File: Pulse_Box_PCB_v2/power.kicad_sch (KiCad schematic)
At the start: 30 parts, among them J1 Screw_Terminal_01x02, U3 TPS54560BDDA, U4 AP2112K-3.3, U5 74LVC1G3157

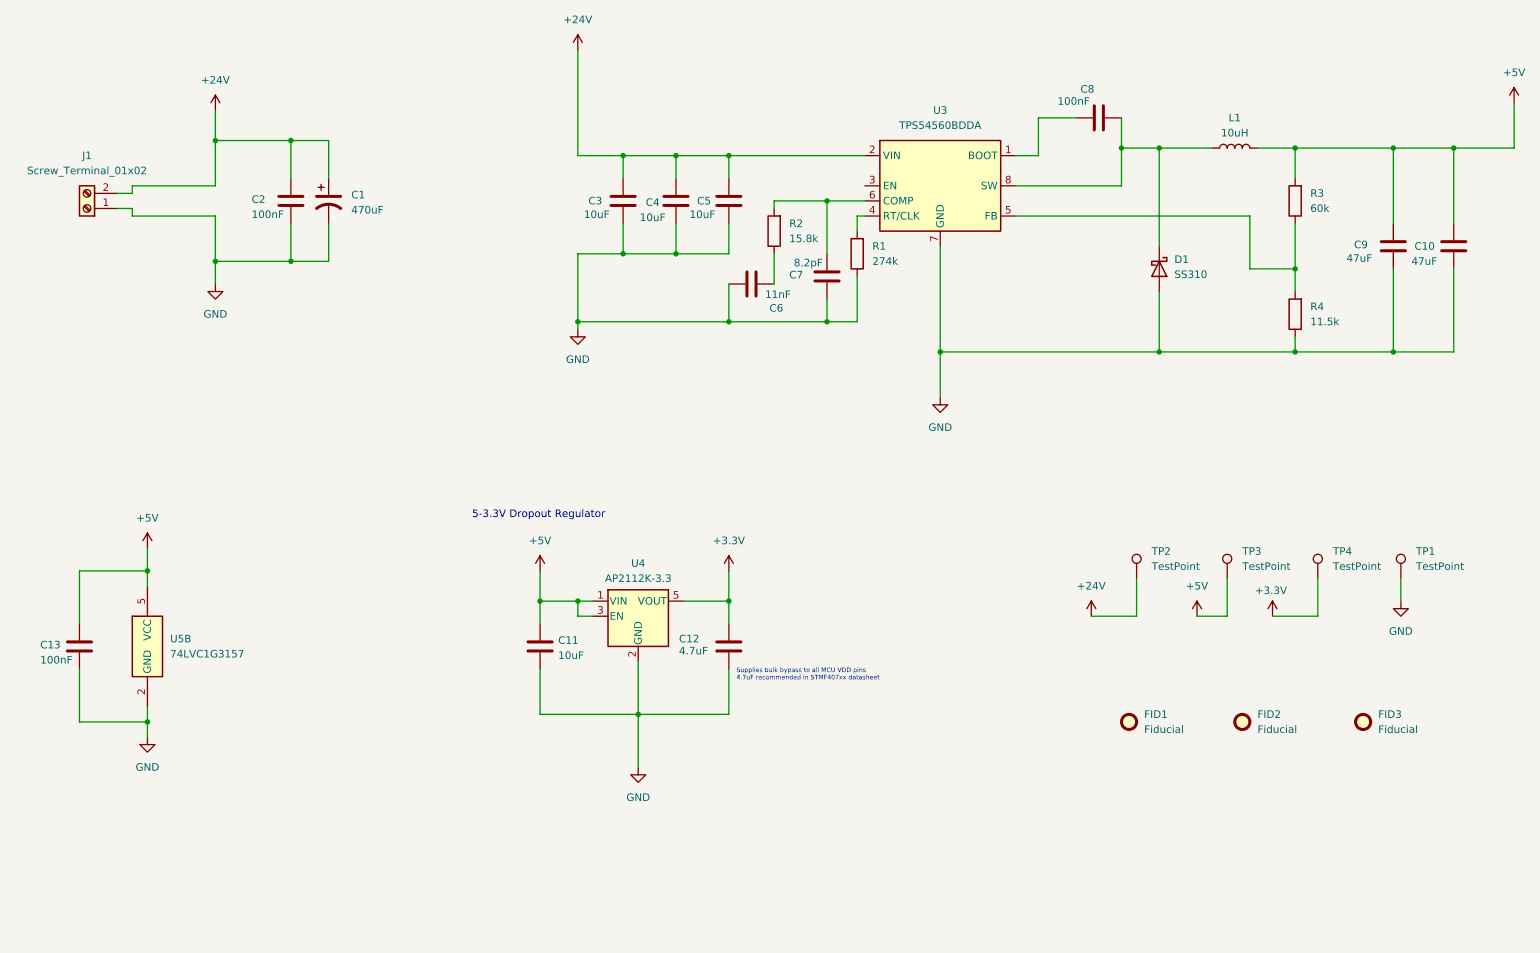
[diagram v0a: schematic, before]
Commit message: add design for pulsebox panel, update v2 PCB to remove 485 trans
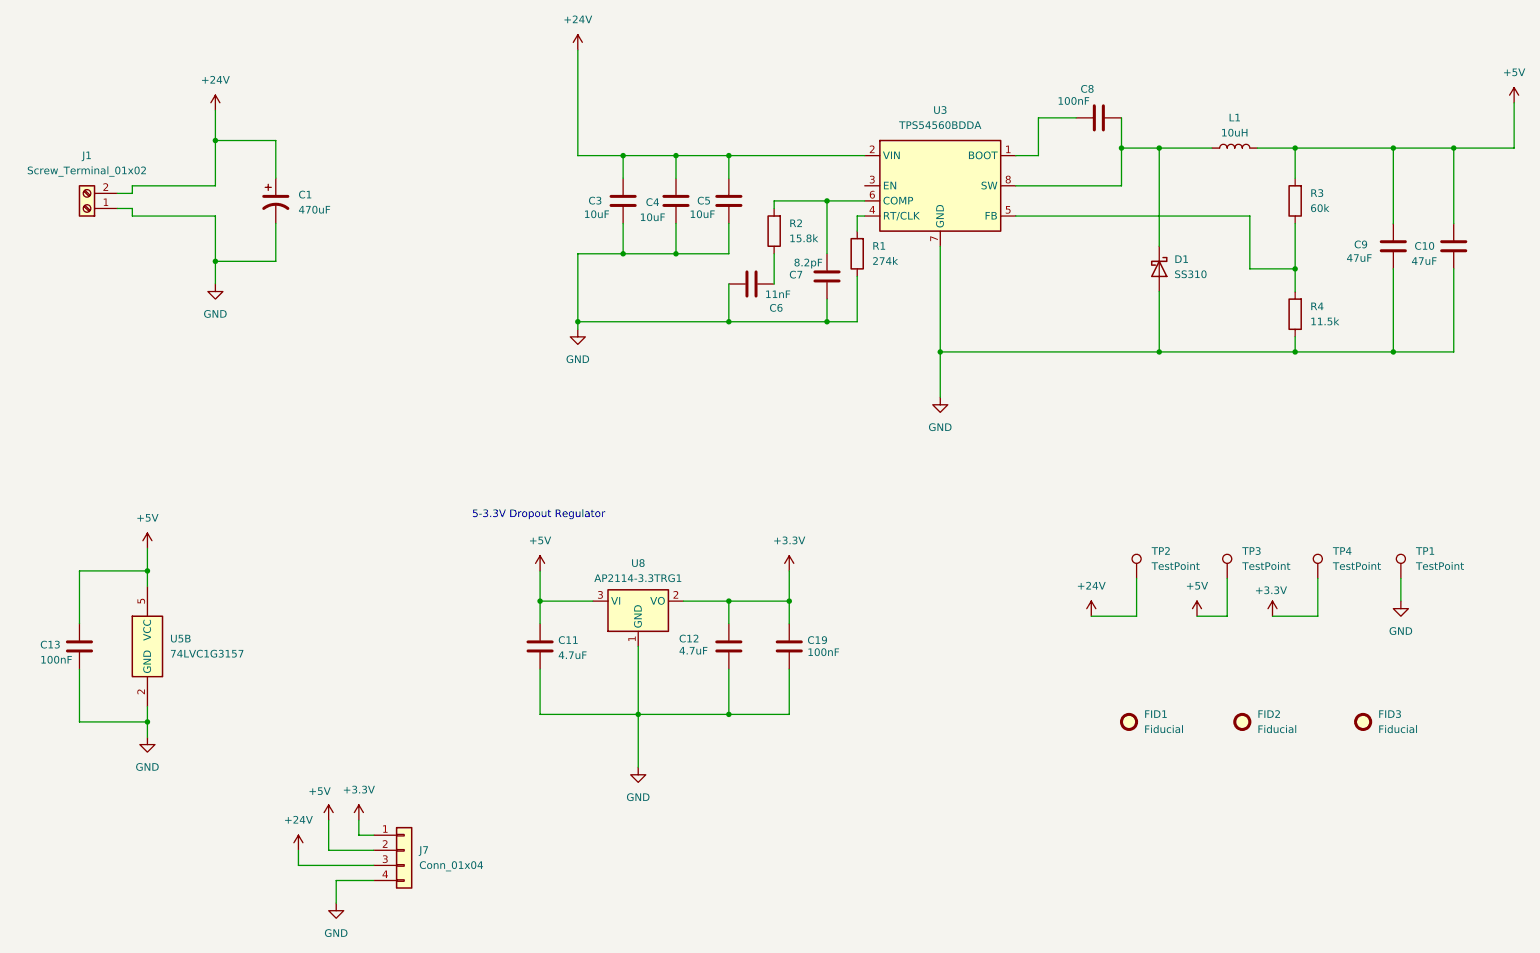
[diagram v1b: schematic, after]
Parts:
- removed C2: 100nF, Capacitor_SMD:C_0402_1005Metric, symbol Device:C
- removed U4: AP2112K-3.3, Package_TO_SOT_SMD:SOT-23-5, symbol Regulator_Linear:AP2112K-3.3
- added C19: 100nF, Capacitor_SMD:C_0402_1005Metric, symbol Device:C
- added J7: Conn_01x04, Connector_PinHeader_2.54mm:PinHeader_1x04_P2.54mm_Vertical, symbol Connector_Generic:Conn_01x04
- added U8: AP2114-3.3TRG1, Package_TO_SOT_SMD:SOT-223-3_TabPin2, symbol Regulator_Linear:AP1117-33
- C11: value 10uF -> 4.7uF; JLCPCB Part # C440198 -> C1779
- C6: footprint Capacitor_SMD:C_1206_3216Metric -> Capacitor_SMD:C_0805_2012Metric; JLCPCB Part # C2171071 -> C710944
- U5: footprint (none) -> Package_TO_SOT_SMD:SOT-23-6; JLCPCB Part # C52140494 -> C10426
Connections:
- net +24V: now also J7.3 (Pin_3)
- net +3.3V: now also C19.1, J7.1 (Pin_1), U8.2 (VO)
- net +5V: now also J7.2 (Pin_2), U8.3 (VI)
- net GND: now also C19.2, J7.4 (Pin_4), U8.1 (GND)
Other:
- note removed: "Supplies bulk bypass to all MCU VDD pins 4.7uF recommended in STMF407xx datasheet"
- moved on the sheet: C1

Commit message: complete v2 and v1 panel design, this is the final design sent to jlcpcb for v2
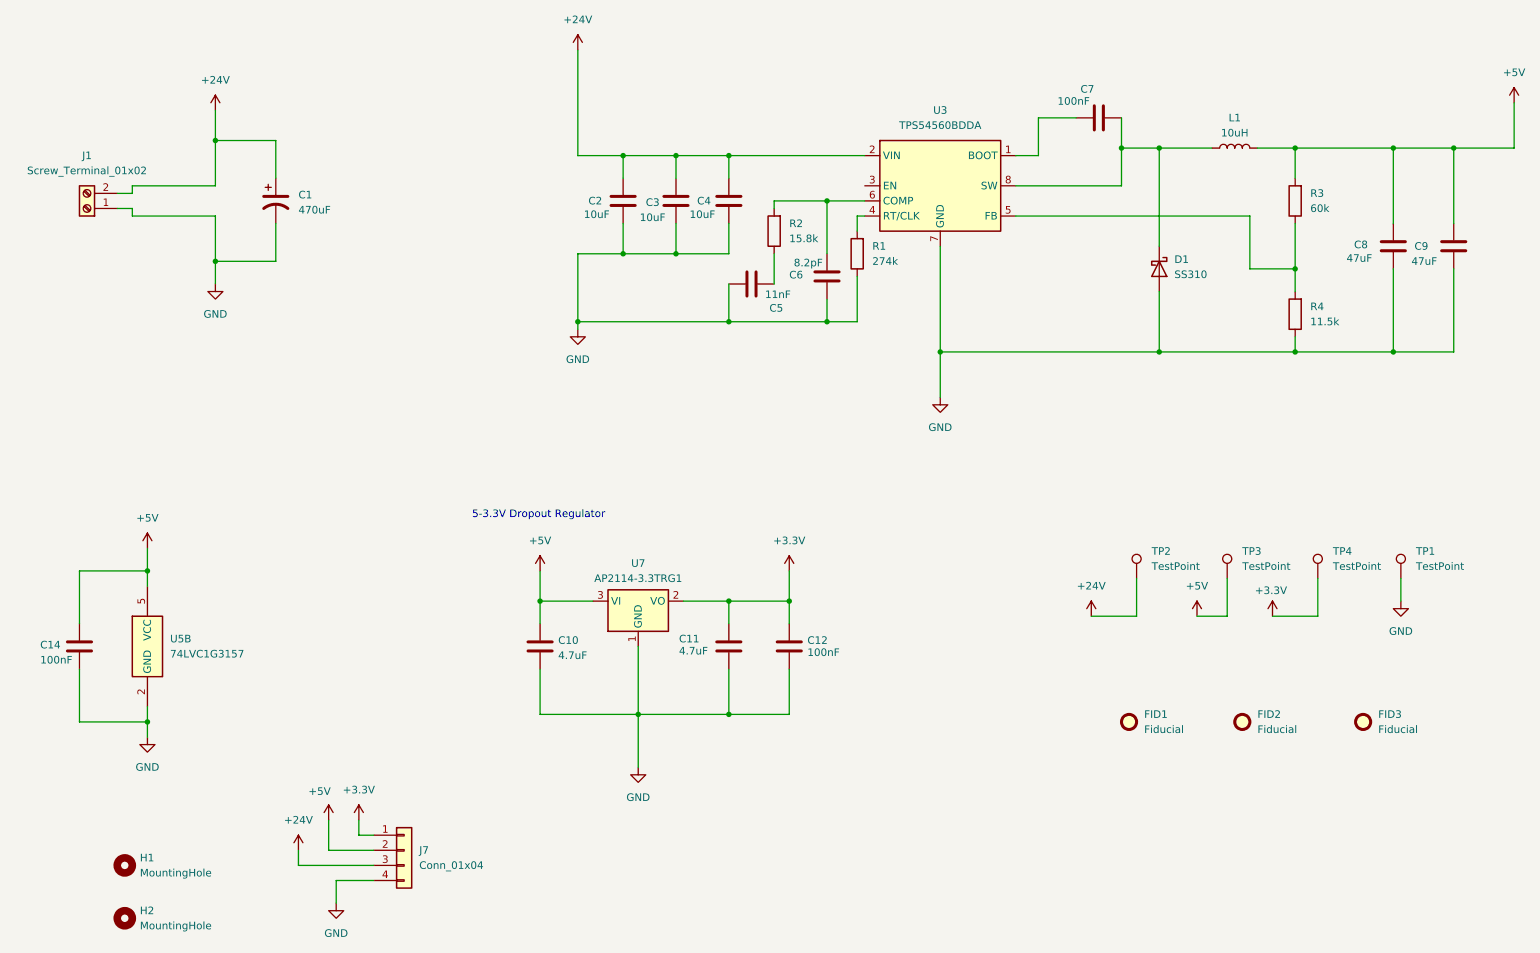
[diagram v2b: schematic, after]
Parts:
- added H1, H2: MountingHole, MountingHole:MountingHole_3.2mm_M3, symbol Mechanical:MountingHole
- L1: footprint Inductor_SMD:L_APV_APH1030 -> Inductor_SMD:L_TechFuse_SL1040
- renumbered C11 to C10, C12 to C11, C19 to C12, C13 to C14, C3 to C2, C4 to C3, C5 to C4, C6 to C5, C7 to C6, C8 to C7, C9 to C8, C10 to C9, U8 to U7
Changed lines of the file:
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@@
 	)
 	(symbol
+		(lib_id "Mechanical:MountingHole")
+		(at 39.37 173.99 0)
+		(unit 1)
+		(exclude_from_sim no)
+		(in_bom no)
+		(on_board yes)
+		(dnp no)
+		(fields_autoplaced yes)
+		(property "Reference" "H1"
+			(at 41.91 172.7199 0)
+			(effects
+				(font
+					(size 1.27 1.27)
+				)
+				(justify left)
+			)
+		)
+		(property "Value" "MountingHole"
+			(at 41.91 175.2599 0)
+			(effects
+				(font
+					(size 1.27 1.27)
+				)
+				(justify left)
+			)
+		)
+		(property "Footprint" "MountingHole:MountingHole_3.2mm_M3"
+			(at 39.37 173.99 0)
+			(effects
+				(font
+					(size 1.27 1.27)
+				)
+				(hide yes)
+			)
+		)
+		(property "Datasheet" "~"
+			(at 39.37 173.99 0)
+			(effects
+				(font
+					(size 1.27 1.27)
+				)
+				(hide yes)
+			)
+		)
+		(property "Description" "Mounting Hole without connection"
+			(at 39.37 173.99 0)
+			(effects
+				(font
+					(size 1.27 1.27)
+				)
+				(hide yes)
+			)
+		)
+		(instances
+			(project ""
+				(path "/ef0e555f-a8f1-4b4b-84db-9e9da0748d24/ac0dde2f-bbaa-42bf-826d-318675a6462a"
+					(reference "H1")
+					(unit 1)
+				)
+			)
+		)
+	)
+	(symbol
 		(lib_id "power:+5V")
 		(at 73.66 166.37 0)
@@
 	)
 	(symbol
+		(lib_id "Mechanical:MountingHole")
+		(at 39.37 182.88 0)
+		(unit 1)
+		(exclude_from_sim no)
+		(in_bom no)
+		(on_board yes)
+		(dnp no)
+		(fields_autoplaced yes)
+		(property "Reference" "H2"
+			(at 41.91 181.6099 0)
+			(effects
+				(font
+					(size 1.27 1.27)
+				)
+				(justify left)
+			)
+		)
+		(property "Value" "MountingHole"
+			(at 41.91 184.1499 0)
+			(effects
+				(font
+					(size 1.27 1.27)
+				)
+				(justify left)
+			)
+		)
+		(property "Footprint" "MountingHole:MountingHole_3.2mm_M3"
+			(at 39.37 182.88 0)
+			(effects
+				(font
+					(size 1.27 1.27)
+				)
+				(hide yes)
+			)
+		)
+		(property "Datasheet" "~"
+			(at 39.37 182.88 0)
+			(effects
+				(font
+					(size 1.27 1.27)
+				)
+				(hide yes)
+			)
+		)
+		(property "Description" "Mounting Hole without connection"
+			(at 39.37 182.88 0)
+			(effects
+				(font
+					(size 1.27 1.27)
+				)
+				(hide yes)
+			)
+		)
+		(instances
+			(project "Pulse_Box_PCB_v2"
+				(path "/ef0e555f-a8f1-4b4b-84db-9e9da0748d24/ac0dde2f-bbaa-42bf-826d-318675a6462a"
+					(reference "H2")
+					(unit 1)
+				)
+			)
+		)
+	)
+	(symbol
 		(lib_id "Device:R")
 		(at 148.59 67.31 180)
@@
 		(on_board yes)
 		(dnp no)
-		(property "Reference" "C8"
+		(property "Reference" "C7"
 			(at 202.438 43.434 90)
 			(effects
@@
 			(project "Pulse_Box_PCB_v2"
 				(path "/ef0e555f-a8f1-4b4b-84db-9e9da0748d24/ac0dde2f-bbaa-42bf-826d-318675a6462a"
-					(reference "C8")
+					(reference "C7")
 					(unit 1)
 				)
@@
 		(on_board yes)
 		(dnp no)
-		(property "Reference" "C3"
+		(property "Reference" "C2"
 			(at 117.348 62.23 0)
 			(effects
@@
 			(project "Pulse_Box_PCB_v2"
 				(path "/ef0e555f-a8f1-4b4b-84db-9e9da0748d24/ac0dde2f-bbaa-42bf-826d-318675a6462a"
-					(reference "C3")
+					(reference "C2")
 					(unit 1)
 				)
@@
 		(on_board yes)
 		(dnp no)
-		(property "Reference" "C12"
+		(property "Reference" "C11"
 			(at 132.588 135.89 0)
 			(effects
@@
 			(project "Pulse_Box_PCB_v2"
 				(path "/ef0e555f-a8f1-4b4b-84db-9e9da0748d24/ac0dde2f-bbaa-42bf-826d-318675a6462a"
-					(reference "C12")
+					(reference "C11")
 					(unit 1)
 				)
@@
 		(on_board yes)
 		(dnp no)
-		(property "Reference" "C19"
+		(property "Reference" "C12"
 			(at 154.178 136.144 0)
 			(effects
@@
 			(project "Pulse_Box_PCB_v2"
 				(path "/ef0e555f-a8f1-4b4b-84db-9e9da0748d24/ac0dde2f-bbaa-42bf-826d-318675a6462a"
-					(reference "C19")
+					(reference "C12")
 					(unit 1)
 				)
@@
 		(on_board yes)
 		(dnp no)
-		(property "Reference" "C6"
+		(property "Reference" "C5"
 			(at 150.114 80.264 90)
 			(effects
@@
 			(project "Pulse_Box_PCB_v2"
 				(path "/ef0e555f-a8f1-4b4b-84db-9e9da0748d24/ac0dde2f-bbaa-42bf-826d-318675a6462a"
-					(reference "C6")
+					(reference "C5")
 					(unit 1)
 				)
@@
 		(on_board yes)
 		(dnp no)
-		(property "Reference" "C9"
+		(property "Reference" "C8"
 			(at 246.126 69.596 0)
 			(effects
@@
 			(project "Pulse_Box_PCB_v2"
 				(path "/ef0e555f-a8f1-4b4b-84db-9e9da0748d24/ac0dde2f-bbaa-42bf-826d-318675a6462a"
-					(reference "C9")
+					(reference "C8")
 					(unit 1)
 				)
@@
 			)
 		)
-		(property "Footprint" "Inductor_SMD:L_APV_APH1030"
+		(property "Footprint" "Inductor_SMD:L_TechFuse_SL1040"
 			(at 226.06 53.34 0)
 			(effects
@@
 		(on_board yes)
 		(dnp no)
-		(property "Reference" "C7"
+		(property "Reference" "C6"
 			(at 151.13 74.676 0)
 			(effects
@@
 			(project "Pulse_Box_PCB_v2"
 				(path "/ef0e555f-a8f1-4b4b-84db-9e9da0748d24/ac0dde2f-bbaa-42bf-826d-318675a6462a"
-					(reference "C7")
+					(reference "C6")
 					(unit 1)
 				)
@@
 		(on_board yes)
 		(dnp no)
-		(property "Reference" "C4"
+		(property "Reference" "C3"
 			(at 127 62.484 0)
 			(effects
@@
 			(project "Pulse_Box_PCB_v2"
 				(path "/ef0e555f-a8f1-4b4b-84db-9e9da0748d24/ac0dde2f-bbaa-42bf-826d-318675a6462a"
-					(reference "C4")
+					(reference "C3")
 					(unit 1)
 				)
@@
 		(on_board yes)
 		(dnp no)
-		(property "Reference" "C13"
+		(property "Reference" "C14"
 			(at 25.146 136.906 0)
 			(effects
@@
 			(project "Pulse_Box_PCB_v2"
 				(path "/ef0e555f-a8f1-4b4b-84db-9e9da0748d24/ac0dde2f-bbaa-42bf-826d-318675a6462a"
-					(reference "C13")
+					(reference "C14")
 					(unit 1)
 				)
@@
 		(on_board yes)
 		(dnp no)
-		(property "Reference" "C10"
+		(property "Reference" "C9"
 			(at 256.286 69.85 0)
 			(effects
@@
 			(project "Pulse_Box_PCB_v2"
 				(path "/ef0e555f-a8f1-4b4b-84db-9e9da0748d24/ac0dde2f-bbaa-42bf-826d-318675a6462a"
-					(reference "C10")
+					(reference "C9")
 					(unit 1)
 				)
@@
 		(on_board yes)
 		(dnp no)
-		(property "Reference" "C11"
+		(property "Reference" "C10"
 			(at 112.268 136.144 0)
 			(effects
@@
 			(project "Pulse_Box_PCB_v2"
 				(path "/ef0e555f-a8f1-4b4b-84db-9e9da0748d24/ac0dde2f-bbaa-42bf-826d-318675a6462a"
-					(reference "C11")
+					(reference "C10")
 					(unit 1)
 				)
@@
 		(on_board yes)
 		(dnp no)
-		(property "Reference" "C5"
+		(property "Reference" "C4"
 			(at 135.636 62.23 0)
 			(effects
@@
 			(project "Pulse_Box_PCB_v2"
 				(path "/ef0e555f-a8f1-4b4b-84db-9e9da0748d24/ac0dde2f-bbaa-42bf-826d-318675a6462a"
-					(reference "C5")
+					(reference "C4")
 					(unit 1)
 				)
@@
 		(dnp no)
 		(fields_autoplaced yes)
-		(property "Reference" "U8"
+		(property "Reference" "U7"
 			(at 125.73 123.19 0)
 			(effects
@@
 			(project ""
 				(path "/ef0e555f-a8f1-4b4b-84db-9e9da0748d24/ac0dde2f-bbaa-42bf-826d-318675a6462a"
-					(reference "U8")
+					(reference "U7")
 					(unit 1)
 				)
